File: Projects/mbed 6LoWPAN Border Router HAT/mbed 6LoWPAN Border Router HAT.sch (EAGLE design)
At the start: 84 parts, among them CON1 TC2030-CTX-NL, CON2 USB_MICROB, IC1 CAT24C32WI-GT3, IC2 74LVC1GXX, IC3 MK64FN1M0VLL12, IC4 LPC11U35FHI33/501, IC5 USBLC6-2SC6, IC6 LD1117S33, Q1 32.768kHz, Q2 12MHz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

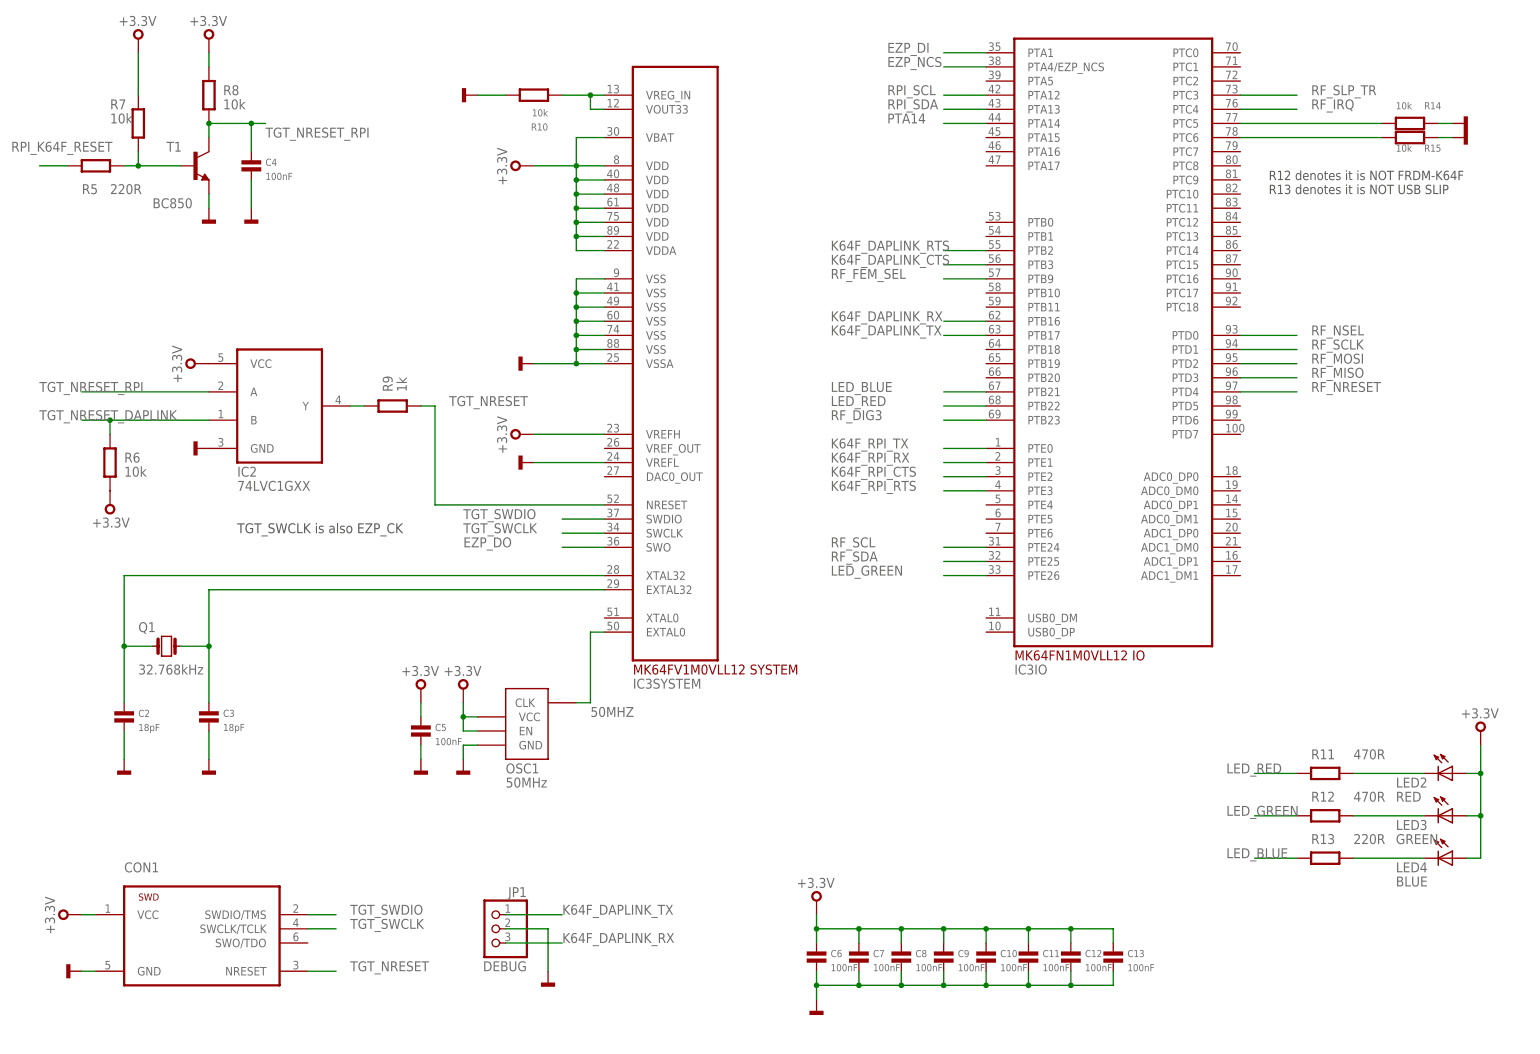
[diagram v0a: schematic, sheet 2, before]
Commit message: Rev 1.1 for 6LoWPAN Border Router Hat
Update Gerbers

Cleaned Schematic

Cleaned up silk screen

Updated sch and brd for final build

Added all output CAM files V_1_1

Final version V_1_1 of Border Router Hat Job

Updated ignore files
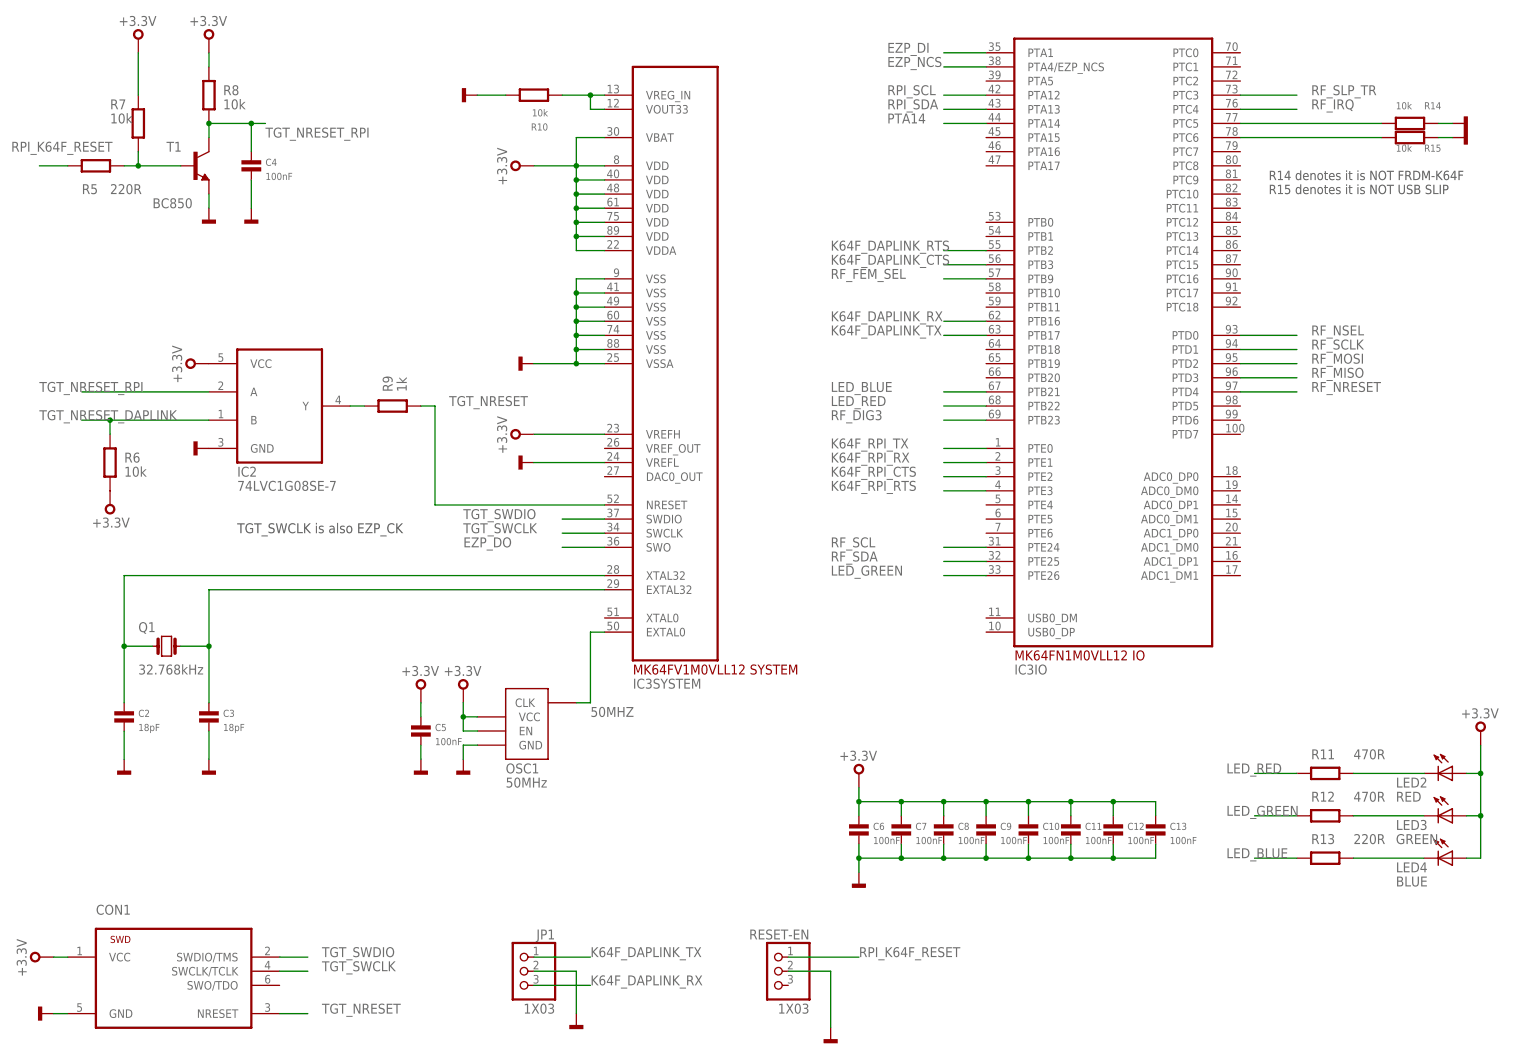
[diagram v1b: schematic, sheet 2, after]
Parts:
- added RESET-EN: 1X03, mbed-HDK:PINHD-1X3
- IC2: value 74LVC1GXX -> 74LVC1G08SE-7
- JP1: value DEBUG -> 1X03
- R21: value 470R -> 220R
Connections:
- net GND: now also RESET-EN.2
- net RPI_K64F_RESET: now also RESET-EN.1
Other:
- note added: "R14 denotes it is NOT FRDM-K64F R15 denotes it is NOT USB SLIP"
- note removed: "R12 denotes it is NOT FRDM-K64F R13 denotes it is NOT USB SLIP"
- moved on the sheet: C10, C11, C12, C13, C6, C7, C8, C9, CON1, JP1
